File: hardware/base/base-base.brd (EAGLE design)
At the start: 76.2 x 101.3 mm, 30 parts, among them U1 SD_CARD_SOCKET4UCON, X1 BU-SMA-1-7HOLE

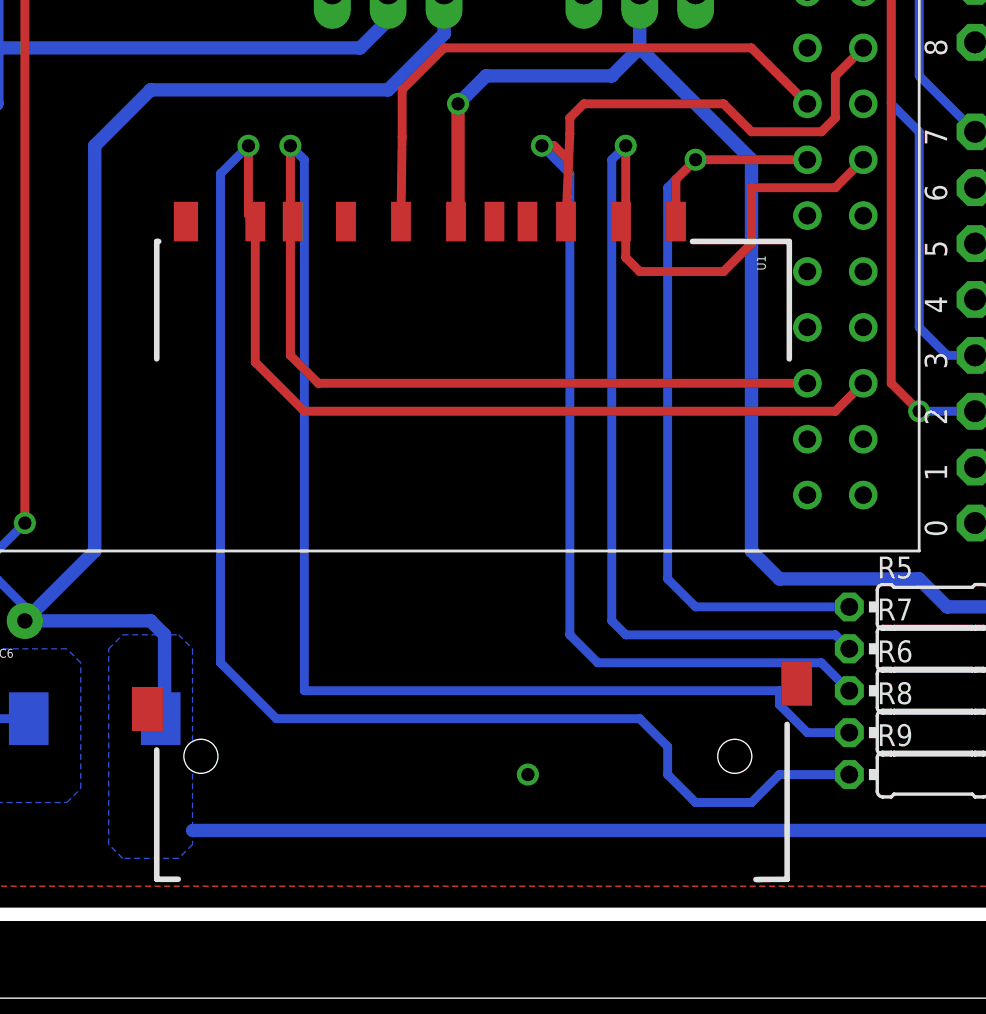
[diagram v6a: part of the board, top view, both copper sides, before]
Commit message: BASEHW: New SD footprint
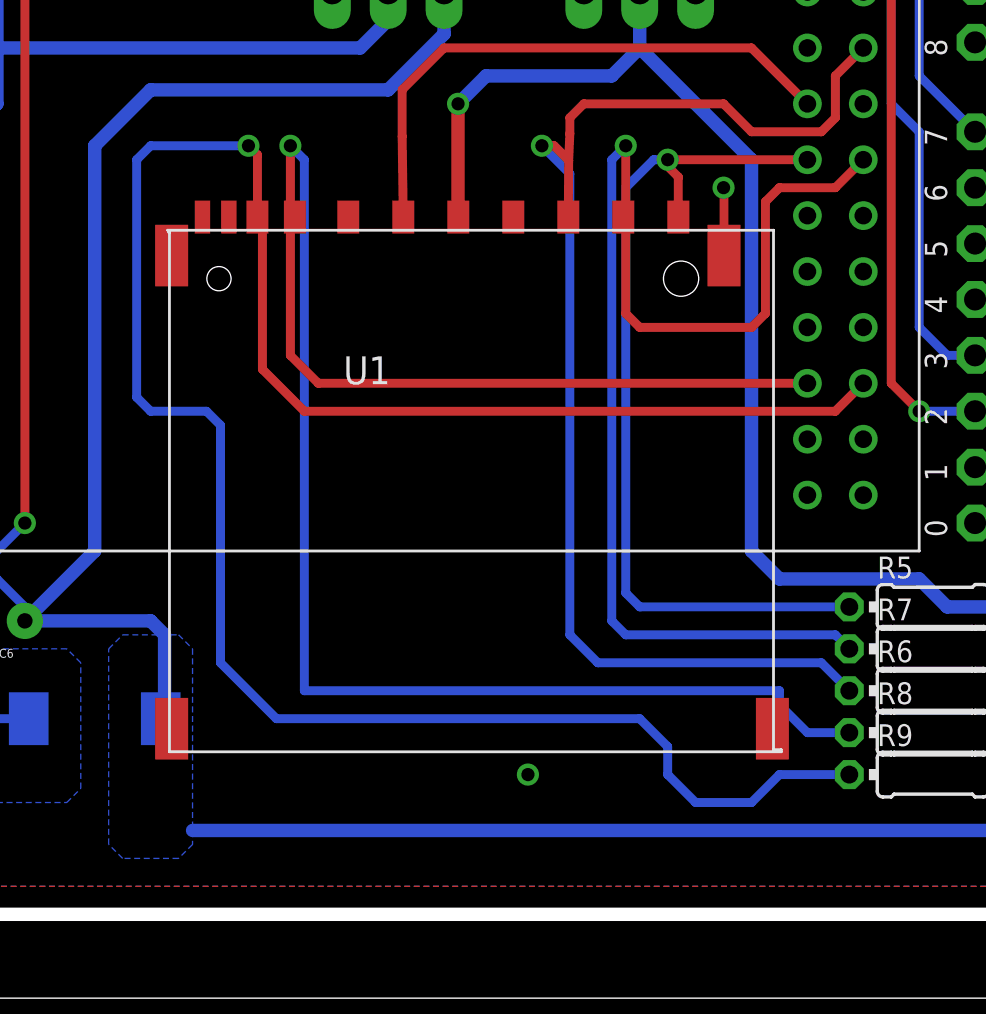
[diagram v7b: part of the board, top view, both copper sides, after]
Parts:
- U1: value SD_CARD_SOCKET4UCON -> SD_CARD_SOCKET2041021FFROMTESIFOPEN; device SparkFun-Connectors:SDCARD_4UCONN -> FullyCustom:SDCARD_2041021-3
- moved U1 23.5 mm to (44.5, 10.8), turned to 0 degrees
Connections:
- net GND: now also U1.SH1, U1.SH2, U1.SH3, U1.SH4; no longer U1.SH@1, U1.SH@2
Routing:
- net SD_DAT1: track 95.5 -> 102.8 mm
- net SD_DAT3: track 53.1 -> 58.1 mm
- net SD_DAT2: track 36.6 -> 40.4 mm
- net GND: track 168.3 -> 171.4 mm, vias 6 -> 7
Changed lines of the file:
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@@
 <element name="U$2" library="Moteino" package="RFM69W-MINPADS" value="RFM69" x="26.67" y="69.85" rot="R270"/>
 <element name="U$3" library="FullyCustom" package="ARDUINO-NOHOLE" value="ARDUINO_GSMSHIELD" x="16.51" y="85.09" rot="R270"/>
-<element name="U1" library="SparkFun-Connectors" package="SDCARD_4UCONN" value="SD_CARD_SOCKET4UCON" x="44.45" y="34.29" rot="R270"/>
+<element name="U1" library="FullyCustom" package="SDCARD_2041021-3" value="SD_CARD_SOCKET2041021FFROMTESIFOPEN" x="44.45" y="10.795"/>
 <element name="X1" library="FullyCustom" package="SMA_1-7HOLES" value="BU-SMA-1-7HOLE" x="40.64" y="80.01" rot="R180">
 <attribute name="OC_NEWARK" value="unknown" x="40.64" y="80.01" size="1.778" layer="27" rot="R180" display="off"/>
@@
 <contactref element="U1" pad="3"/>
 <contactref element="U1" pad="6"/>
-<contactref element="U1" pad="SH@2"/>
-<contactref element="U1" pad="SH@1"/>
 <contactref element="U$3" pad="GND"/>
 <contactref element="U$3" pad="GND1"/>
@@
 <wire x1="10.16" y1="18.415" x2="10.795" y2="18.415" width="0.4064" layer="16"/>
 <wire x1="10.795" y1="18.415" x2="12.065" y2="17.145" width="0.4064" layer="16"/>
+<contactref element="U1" pad="SH1"/>
+<contactref element="U1" pad="SH2"/>
+<contactref element="U1" pad="SH3"/>
+<contactref element="U1" pad="SH4"/>
+<wire x1="55.9" y1="33.745" x2="55.9" y2="36.81" width="0.4064" layer="1"/>
+<wire x1="55.9" y1="36.81" x2="55.88" y2="36.83" width="0.4064" layer="1"/>
+<via x="55.88" y="36.83" extent="1-16" drill="0.6"/>
 </signal>
 <signal name="RADIO_CS">
@@
 <wire x1="37.465" y1="27.94" x2="36.195" y2="29.21" width="0.4064" layer="1"/>
 <contactref element="R8" pad="1"/>
-<wire x1="36.195" y1="29.21" x2="36.195" y2="35.185" width="0.4064" layer="1"/>
-<wire x1="36.195" y1="35.185" x2="36.3" y2="35.29" width="0.4064" layer="1"/>
 <wire x1="58.42" y1="13.97" x2="36.83" y2="13.97" width="0.4064" layer="16"/>
 <wire x1="36.83" y1="13.97" x2="36.83" y2="38.1" width="0.4064" layer="16"/>
@@
 <via x="36.195" y="38.735" extent="1-16" drill="0.6"/>
 <wire x1="36.195" y1="38.735" x2="36.195" y2="35.395" width="0.4064" layer="1"/>
-<wire x1="36.195" y1="35.395" x2="36.3" y2="35.29" width="0.4064" layer="1"/>
+<wire x1="36.195" y1="35.395" x2="36.4" y2="35.495" width="0.4064" layer="1"/>
 <wire x1="58.42" y1="13.97" x2="58.42" y2="13.335" width="0.4064" layer="16"/>
 <wire x1="58.42" y1="13.335" x2="59.69" y2="12.065" width="0.4064" layer="16"/>
 <wire x1="59.69" y1="12.065" x2="61.595" y2="12.065" width="0.4064" layer="16"/>
+<wire x1="36.195" y1="29.21" x2="36.195" y2="35.29" width="0.4064" layer="1"/>
+<wire x1="36.195" y1="35.29" x2="36.4" y2="35.495" width="0.4064" layer="1"/>
 </signal>
 <signal name="SD_DAT1">
@@
 <contactref element="U$1" pad="P$96"/>
 <contactref element="R9" pad="1"/>
-<wire x1="34.6" y1="28.9" x2="36.83" y2="26.67" width="0.4064" layer="1"/>
 <wire x1="36.83" y1="26.67" x2="60.96" y2="26.67" width="0.4064" layer="1"/>
 <wire x1="60.96" y1="26.67" x2="62.23" y2="27.94" width="0.4064" layer="1"/>
-<wire x1="34.6" y1="28.9" x2="34.6" y2="35.29" width="0.4064" layer="1"/>
 <wire x1="35.56" y1="12.7" x2="33.02" y2="15.24" width="0.4064" layer="16"/>
-<wire x1="33.02" y1="15.24" x2="33.02" y2="37.465" width="0.4064" layer="16"/>
-<wire x1="33.02" y1="37.465" x2="34.29" y2="38.735" width="0.4064" layer="16"/>
 <via x="34.29" y="38.735" extent="1-16" drill="0.6"/>
-<wire x1="34.29" y1="38.735" x2="34.29" y2="35.6" width="0.4064" layer="1"/>
-<wire x1="34.29" y1="35.6" x2="34.6" y2="35.29" width="0.4064" layer="1"/>
 <wire x1="61.595" y1="10.16" x2="58.42" y2="10.16" width="0.4064" layer="16"/>
 <wire x1="58.42" y1="10.16" x2="57.15" y2="8.89" width="0.4064" layer="16"/>
@@
 <wire x1="53.34" y1="11.43" x2="52.07" y2="12.7" width="0.4064" layer="16"/>
 <wire x1="52.07" y1="12.7" x2="35.56" y2="12.7" width="0.4064" layer="16"/>
+<wire x1="36.83" y1="26.67" x2="34.925" y2="28.575" width="0.4064" layer="1"/>
+<wire x1="34.925" y1="28.575" x2="34.925" y2="35.27" width="0.4064" layer="1"/>
+<wire x1="34.925" y1="35.27" x2="34.7" y2="35.495" width="0.4064" layer="1"/>
+<wire x1="34.7" y1="35.495" x2="34.7" y2="38.325" width="0.4064" layer="1"/>
+<wire x1="34.7" y1="38.325" x2="34.29" y2="38.735" width="0.4064" layer="1"/>
+<wire x1="34.29" y1="38.735" x2="29.845" y2="38.735" width="0.4064" layer="16"/>
+<wire x1="29.845" y1="38.735" x2="29.21" y2="38.1" width="0.4064" layer="16"/>
+<wire x1="29.21" y1="38.1" x2="29.21" y2="27.305" width="0.4064" layer="16"/>
+<wire x1="29.21" y1="27.305" x2="29.845" y2="26.67" width="0.4064" layer="16"/>
+<wire x1="29.845" y1="26.67" x2="32.385" y2="26.67" width="0.4064" layer="16"/>
+<wire x1="32.385" y1="26.67" x2="33.02" y2="26.035" width="0.4064" layer="16"/>
+<wire x1="33.02" y1="26.035" x2="33.02" y2="15.24" width="0.4064" layer="16"/>
 </signal>
 <signal name="SD_DAT2">
@@
 <contactref element="U$1" pad="P$87"/>
 <contactref element="R5" pad="1"/>
-<wire x1="53.72" y1="35.29" x2="53.72" y2="37.21" width="0.4064" layer="1"/>
-<wire x1="61.595" y1="17.78" x2="54.61" y2="17.78" width="0.4064" layer="16"/>
-<wire x1="54.61" y1="17.78" x2="53.34" y2="19.05" width="0.4064" layer="16"/>
-<wire x1="53.34" y1="19.05" x2="53.34" y2="36.83" width="0.4064" layer="16"/>
-<wire x1="53.34" y1="36.83" x2="54.61" y2="38.1" width="0.4064" layer="16"/>
-<via x="54.61" y="38.1" extent="1-16" drill="0.6"/>
-<wire x1="54.61" y1="38.1" x2="59.69" y2="38.1" width="0.4064" layer="1"/>
-<wire x1="53.72" y1="37.21" x2="54.61" y2="38.1" width="0.4064" layer="1"/>
+<wire x1="61.595" y1="17.78" x2="52.07" y2="17.78" width="0.4064" layer="16"/>
+<via x="53.34" y="38.1" extent="1-16" drill="0.6"/>
+<wire x1="53.34" y1="38.1" x2="59.69" y2="38.1" width="0.4064" layer="1"/>
+<wire x1="53.825" y1="35.495" x2="53.825" y2="37.315" width="0.4064" layer="1"/>
+<wire x1="53.34" y1="38.1" x2="53.34" y2="37.8" width="0.4064" layer="1"/>
+<wire x1="53.34" y1="37.8" x2="53.825" y2="37.315" width="0.4064" layer="1"/>
+<wire x1="51.435" y1="36.83" x2="51.435" y2="18.415" width="0.4064" layer="16"/>
+<wire x1="51.435" y1="18.415" x2="52.07" y2="17.78" width="0.4064" layer="16"/>
+<wire x1="53.34" y1="38.1" x2="52.705" y2="38.1" width="0.4064" layer="16"/>
+<wire x1="52.705" y1="38.1" x2="51.435" y2="36.83" width="0.4064" layer="16"/>
 </signal>
 <signal name="SD_CLK">
@@
 <wire x1="57.15" y1="43.18" x2="43.18" y2="43.18" width="0.4064" layer="1"/>
 <wire x1="41.275" y1="41.275" x2="41.275" y2="39.155" width="0.4064" layer="1"/>
-<wire x1="41.275" y1="39.155" x2="41.22" y2="35.29" width="0.4064" layer="1"/>
+<wire x1="41.275" y1="39.155" x2="41.325" y2="35.495" width="0.4064" layer="1"/>
 </signal>
 <signal name="SD_CMD">
@@
 <wire x1="48.895" y1="39.275" x2="48.842278125" y2="38.074428125" width="0.4064" layer="1"/>
 <contactref element="R6" pad="1"/>
-<wire x1="48.842278125" y1="38.074428125" x2="48.72" y2="35.29" width="0.4064" layer="1"/>
+<wire x1="48.842278125" y1="38.074428125" x2="48.825" y2="35.495" width="0.4064" layer="1"/>
 <wire x1="60.325" y1="15.24" x2="50.165" y2="15.24" width="0.4064" layer="16"/>
 <wire x1="50.165" y1="15.24" x2="48.895" y2="16.51" width="0.4064" layer="16"/>
@@
 <via x="51.435" y="38.735" extent="1-16" drill="0.6"/>
 <wire x1="51.435" y1="38.735" x2="51.435" y2="35.505" width="0.4064" layer="1"/>
-<wire x1="51.435" y1="35.505" x2="51.22" y2="35.29" width="0.4064" layer="1"/>
+<wire x1="51.435" y1="35.505" x2="51.325" y2="35.495" width="0.4064" layer="1"/>
 <wire x1="62.23" y1="38.1" x2="60.96" y2="36.83" width="0.4064" layer="1"/>
-<wire x1="60.96" y1="36.83" x2="57.15" y2="36.83" width="0.4064" layer="1"/>
-<wire x1="57.15" y1="36.83" x2="57.15" y2="34.29" width="0.4064" layer="1"/>
-<wire x1="57.15" y1="34.29" x2="55.88" y2="33.02" width="0.4064" layer="1"/>
-<wire x1="55.88" y1="33.02" x2="52.07" y2="33.02" width="0.4064" layer="1"/>
-<wire x1="52.07" y1="33.02" x2="51.435" y2="33.655" width="0.4064" layer="1"/>
-<wire x1="51.435" y1="33.655" x2="51.435" y2="35.075" width="0.4064" layer="1"/>
-<wire x1="51.435" y1="35.075" x2="51.22" y2="35.29" width="0.4064" layer="1"/>
+<wire x1="51.435" y1="35.075" x2="51.325" y2="35.495" width="0.4064" layer="1"/>
 <wire x1="60.96" y1="16.51" x2="61.595" y2="15.875" width="0.4064" layer="16"/>
+<wire x1="51.435" y1="35.075" x2="51.435" y2="31.115" width="0.4064" layer="1"/>
+<wire x1="51.435" y1="31.115" x2="52.07" y2="30.48" width="0.4064" layer="1"/>
+<wire x1="52.07" y1="30.48" x2="57.15" y2="30.48" width="0.4064" layer="1"/>
+<wire x1="57.15" y1="30.48" x2="57.785" y2="31.115" width="0.4064" layer="1"/>
+<wire x1="57.785" y1="31.115" x2="57.785" y2="36.195" width="0.4064" layer="1"/>
+<wire x1="57.785" y1="36.195" x2="58.42" y2="36.83" width="0.4064" layer="1"/>
+<wire x1="58.42" y1="36.83" x2="60.96" y2="36.83" width="0.4064" layer="1"/>
 </signal>
 <signal name="RESET">
@@
 <via x="43.815" y="40.64" extent="1-16" drill="0.6"/>
 <wire x1="43.815" y1="40.64" x2="43.815" y2="35.385" width="0.6096" layer="1"/>
-<wire x1="43.815" y1="35.385" x2="43.72" y2="35.29" width="0.6096" layer="1"/>
+<wire x1="43.815" y1="35.385" x2="43.825" y2="35.495" width="0.6096" layer="1"/>
 <wire x1="69.215" y1="17.78" x2="66.04" y2="17.78" width="0.6096" layer="16"/>
 <wire x1="66.04" y1="17.78" x2="64.77" y2="19.05" width="0.6096" layer="16"/>

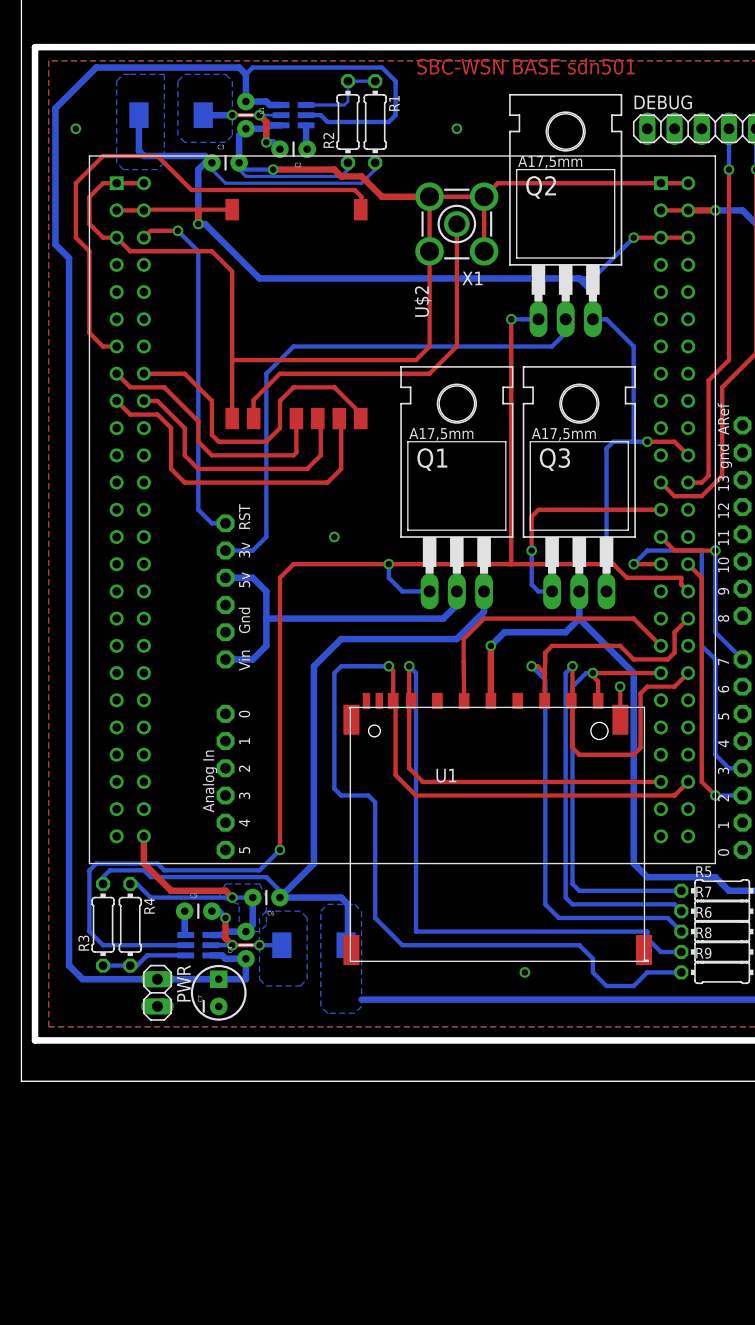
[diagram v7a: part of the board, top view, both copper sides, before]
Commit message: BASEHW: Replaced PSU caps with 1206 parts, added transistor to make MOSFETs work with VREG
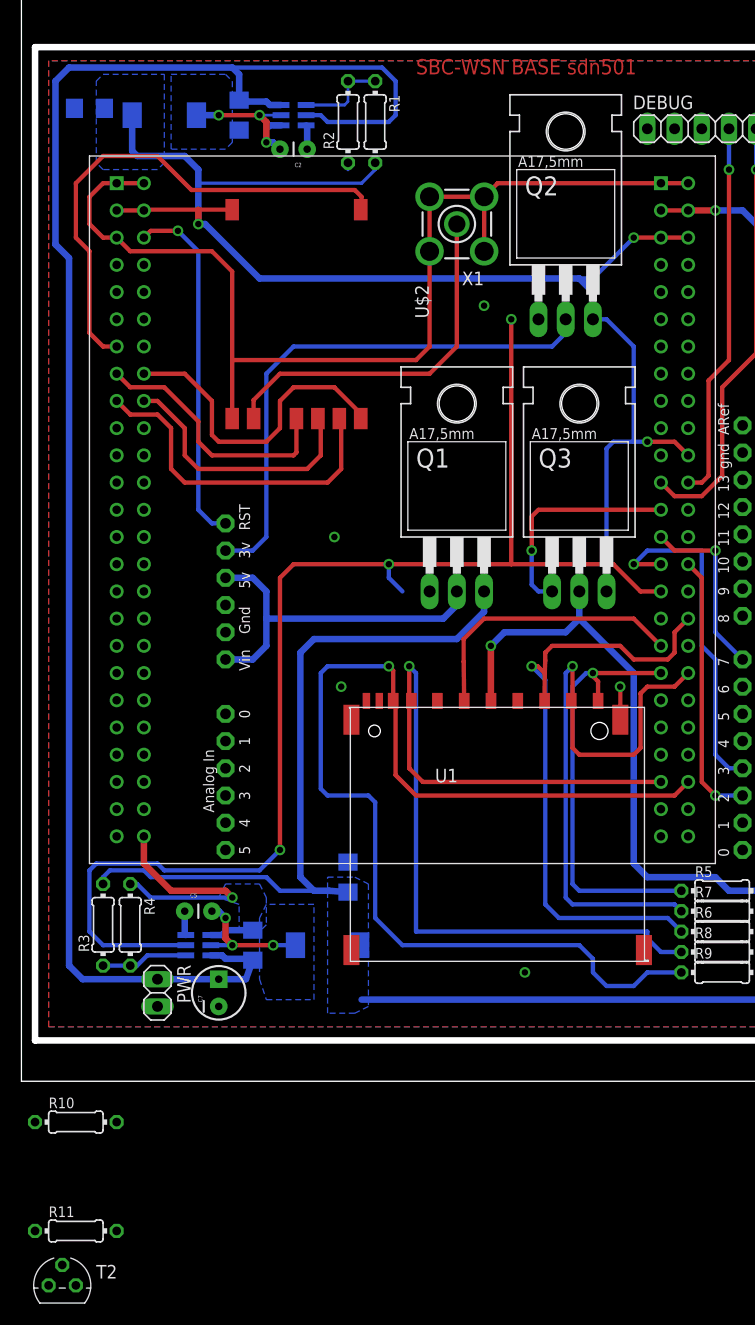
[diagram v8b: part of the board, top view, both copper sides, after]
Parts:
- added R10, R11: 10k, resistor:0204/7
- added T2: BC337, transistor:TO92
- C1, C3, C4, C6: device SparkFun-Capacitors:CAP-PTH-SMALL -> SparkFun-Capacitors:1206
- moved C3 12.5 mm to (6.35, 90.8), flipped to the bottom
- moved C6 6.63 mm to (30.5, 19.1), flipped to the bottom, turned to 90 degrees
- moved C4 1.42 mm to (21.6, 12.7), flipped to the bottom
- moved C1 1.42 mm to (20.3, 90.2), flipped to the bottom
- moved L2 1.27 mm to (28.6, 12.7)
- moved L1 0.63 mm to (13.3, 90.2)
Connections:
- new net GSM_TRANSISTORLINE: Q1.G, Q2.G, R11.1, T2.3
- net +3V3: now also R10.2
- net +5V: now also R11.2
- net GND: now also T2.1
- net GSM_PWR: now also T2.2, U$1.P$81; no longer Q1.G, Q2.G, U$1.P$82
- net SD_PWR: now also R10.1
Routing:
- net GND: track 171.4 -> 131.3 mm, vias 7 -> 6
- net GSM_PWR: track 130.8 -> 122.8 mm
- net V+: track 155.3 -> 158.3 mm
- net SD_DAT1: track 102.8 -> 105.3 mm
- net +3V3: track 136.2 -> 134.4 mm
- net VREG_5_SW: track 11.0 -> 12.2 mm
- net VREG_3_SW: track 11.6 -> 12.2 mm
